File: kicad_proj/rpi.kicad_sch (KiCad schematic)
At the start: 9 parts, among them J4 Raspberry Pi SMT connector, J5 Conn_01x02, U3 CAT24C32WI-GT3

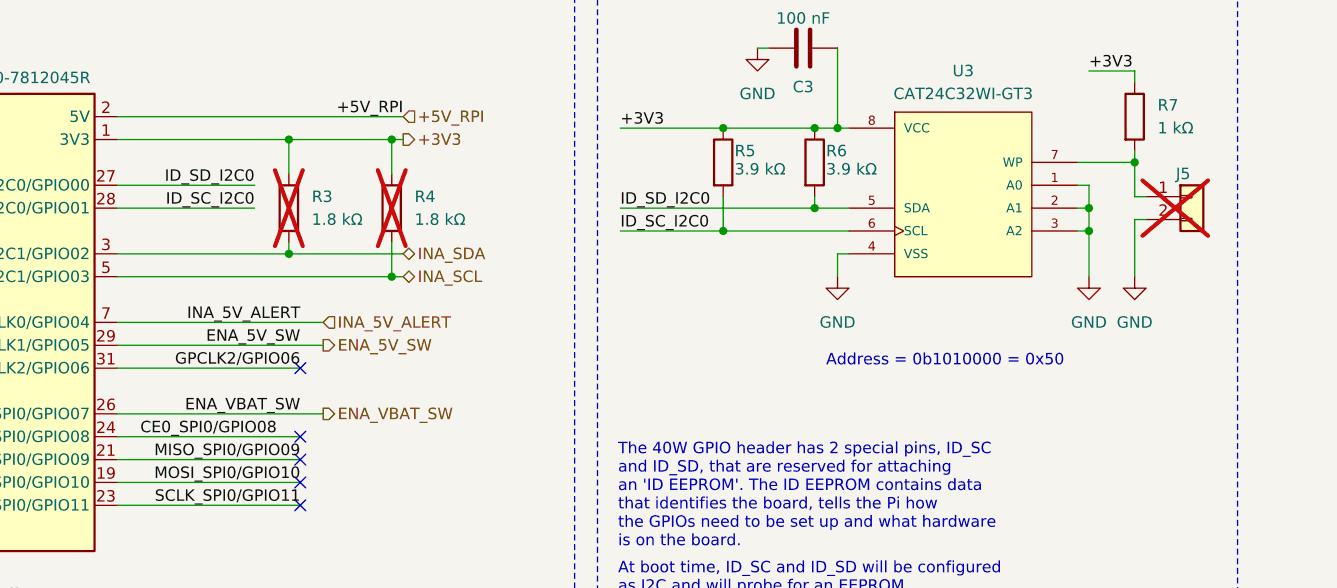
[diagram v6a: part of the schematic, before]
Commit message: feat: replace tht jumper by as solder bridge. feat: progress with layout.
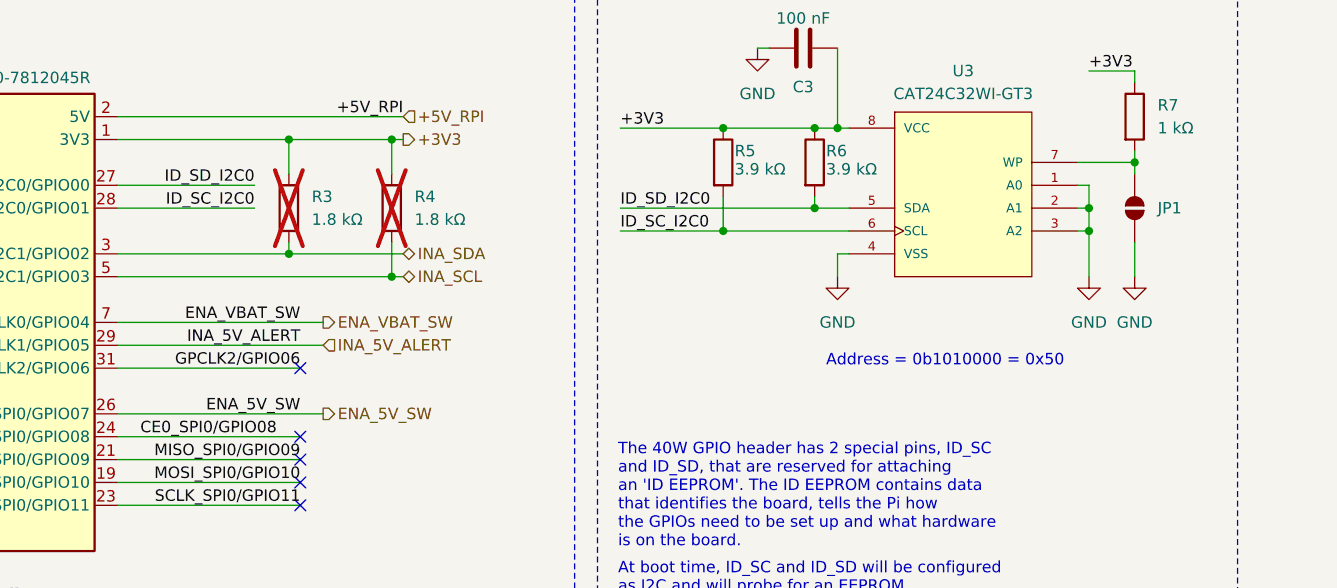
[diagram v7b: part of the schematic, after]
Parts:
- removed J5: Conn_01x02, Connector_PinHeader_2.54mm:PinHeader_1x02_P2.54mm_Vertical, symbol Connector_Generic:Conn_01x02
- added JP1: SolderJumper_2_Open, Jumper:SolderJumper-2_P1.3mm_Open_Pad1.0x1.5mm, symbol Jumper:SolderJumper_2_Open
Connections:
- net ENA_5V_SW: now also J4.26 (~{CE1}_SPI0/GPIO07); no longer J4.29 (GPCLK1/GPIO05)
- net ENA_VBAT_SW: now also J4.7 (GPCLK0/GPIO04); no longer J4.26 (~{CE1}_SPI0/GPIO07)
- net GND: now also JP1.1 (A)
- net INA_5V_ALERT: now also J4.29 (GPCLK1/GPIO05); no longer J4.7 (GPCLK0/GPIO04)
- net at R7.2, U3.7 (WP): now also JP1.2 (B)
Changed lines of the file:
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@@
 	(wire
 		(pts
-			(xy 236.22 63.5) (xy 234.95 63.5)
-		)
-		(stroke
-			(width 0)
-			(type default)
-		)
-	)
-	(wire
-		(pts
 			(xy 229.87 49.53) (xy 234.95 49.53)
 		)
@@
 	(wire
 		(pts
-			(xy 121.92 80.01) (xy 144.78 80.01)
-		)
-		(stroke
-			(width 0)
-			(type default)
-		)
-	)
-	(wire
-		(pts
 			(xy 33.02 77.47) (xy 55.88 77.47)
 		)
@@
 	(wire
 		(pts
-			(xy 234.95 66.04) (xy 234.95 72.39)
+			(xy 189.23 63.5) (xy 189.23 67.31)
 		)
 		(stroke
@@
 	(wire
 		(pts
-			(xy 189.23 63.5) (xy 189.23 67.31)
+			(xy 121.92 80.01) (xy 144.78 80.01)
 		)
 		(stroke
@@
 	(wire
 		(pts
+			(xy 121.92 77.47) (xy 144.78 77.47)
+		)
+		(stroke
+			(width 0)
+			(type default)
+		)
+	)
+	(wire
+		(pts
 			(xy 229.87 72.39) (xy 229.87 67.31)
 		)
@@
 	(wire
 		(pts
-			(xy 121.92 64.77) (xy 137.16 64.77)
+			(xy 234.95 68.58) (xy 234.95 72.39)
 		)
 		(stroke
@@
 	(wire
 		(pts
-			(xy 33.02 95.25) (xy 55.88 95.25)
+			(xy 121.92 87.63) (xy 144.78 87.63)
 		)
 		(stroke
@@
 	(wire
 		(pts
-			(xy 140.97 57.15) (xy 140.97 60.96)
+			(xy 121.92 64.77) (xy 137.16 64.77)
 		)
 		(stroke
@@
 	(wire
 		(pts
-			(xy 177.8 67.31) (xy 189.23 67.31)
+			(xy 33.02 95.25) (xy 55.88 95.25)
 		)
 		(stroke
@@
 	(wire
 		(pts
-			(xy 33.02 80.01) (xy 55.88 80.01)
+			(xy 140.97 57.15) (xy 140.97 60.96)
 		)
 		(stroke
@@
 	(wire
 		(pts
-			(xy 121.92 97.79) (xy 142.24 97.79)
+			(xy 177.8 67.31) (xy 189.23 67.31)
 		)
 		(stroke
@@
 	(wire
 		(pts
-			(xy 234.95 66.04) (xy 236.22 66.04)
+			(xy 33.02 80.01) (xy 55.88 80.01)
 		)
 		(stroke
@@
 	(wire
 		(pts
-			(xy 121.92 87.63) (xy 144.78 87.63)
+			(xy 121.92 97.79) (xy 142.24 97.79)
 		)
 		(stroke
@@
 	(wire
 		(pts
-			(xy 121.92 77.47) (xy 144.78 77.47)
+			(xy 234.95 60.96) (xy 234.95 59.69)
 		)
 		(stroke
@@
 	(wire
 		(pts
-			(xy 234.95 63.5) (xy 234.95 59.69)
-		)
-		(stroke
-			(width 0)
-			(type default)
-		)
-	)
-	(wire
-		(pts
 			(xy 201.93 72.39) (xy 201.93 69.85)
 		)
@@
 		)
 	)
-	(label "INA_5V_ALERT"
-		(at 142.24 77.47 180)
-		(effects
-			(font
-				(size 1.27 1.27)
-			)
-			(justify right bottom)
-		)
-	)
 	(label "GPIO12{slash}PWM0"
 		(at 33.02 54.61 0)
@@
 		)
 	)
-	(label "ENA_VBAT_SW"
-		(at 142.24 87.63 180)
-		(effects
-			(font
-				(size 1.27 1.27)
-			)
-			(justify right bottom)
-		)
-	)
 	(label "ID_SD_I2C0"
 		(at 137.16 62.23 180)
@@
 		)
 	)
+	(label "ENA_VBAT_SW"
+		(at 142.24 77.47 180)
+		(effects
+			(font
+				(size 1.27 1.27)
+			)
+			(justify right bottom)
+		)
+	)
+	(label "INA_5V_ALERT"
+		(at 142.24 80.01 180)
+		(effects
+			(font
+				(size 1.27 1.27)
+			)
+			(justify right bottom)
+		)
+	)
 	(label "ID_SD_I2C0"
 		(at 177.8 64.77 0)
@@
 		)
 	)
-	(label "INA_VBAT_ALERT"
-		(at 33.02 72.39 0)
+	(label "ENA_5V_SW"
+		(at 142.24 87.63 180)
 		(effects
 			(font
 				(size 1.27 1.27)
 			)
-			(justify left bottom)
+			(justify right bottom)
 		)
 	)
-	(label "GPIO15{slash}UART_RXD"
-		(at 33.02 64.77 0)
+	(label "INA_VBAT_ALERT"
+		(at 33.02 72.39 0)
 		(effects
 			(font
@@
 		)
 	)
-	(label "ENA_5V_SW"
-		(at 142.24 80.01 180)
+	(label "GPIO15{slash}UART_RXD"
+		(at 33.02 64.77 0)
 		(effects
 			(font
 				(size 1.27 1.27)
 			)
-			(justify right bottom)
+			(justify left bottom)
 		)
 	)
@@
 		)
 	)
-	(hierarchical_label "INA_VBAT_ALERT"
+	(hierarchical_label "INA_5V_ALERT"
 		(shape input)
-		(at 33.02 72.39 180)
+		(at 144.78 80.01 0)
 		(effects
 			(font
 				(size 1.27 1.27)
 			)
-			(justify right)
+			(justify left)
 		)
 	)
-	(hierarchical_label "INA_SCL"
-		(shape bidirectional)
-		(at 153.67 72.39 0)
+	(hierarchical_label "ENA_VBAT_SW"
+		(shape output)
+		(at 144.78 77.47 0)
 		(effects
 			(font
@@
 		)
 	)
-	(hierarchical_label "ENA_5V_SW"
-		(shape output)
-		(at 144.78 80.01 0)
+	(hierarchical_label "INA_VBAT_ALERT"
+		(shape input)
+		(at 33.02 72.39 180)
 		(effects
 			(font
 				(size 1.27 1.27)
 			)
-			(justify left)
+			(justify right)
 		)
 	)
-	(hierarchical_label "INA_5V_ALERT"
-		(shape input)
-		(at 144.78 77.47 0)
+	(hierarchical_label "INA_SCL"
+		(shape bidirectional)
+		(at 153.67 72.39 0)
 		(effects
 			(font
@@
 		)
 	)
-	(hierarchical_label "ENA_VBAT_SW"
+	(hierarchical_label "ENA_5V_SW"
 		(shape output)
 		(at 144.78 87.63 0)
@@
 	)
 	(symbol
-		(lib_id "Connector_Generic:Conn_01x02")
-		(at 241.3 63.5 0)
+		(lib_id "Jumper:SolderJumper_2_Open")
+		(at 234.95 64.77 90)
 		(unit 1)
-		(exclude_from_sim no)
+		(exclude_from_sim yes)
 		(in_bom no)
 		(on_board yes)
-		(dnp yes)
-		(property "Reference" "J5"
-			(at 239.522 60.96 0)
+		(dnp no)
+		(fields_autoplaced yes)
+		(property "Reference" "JP1"
+			(at 237.49 64.7699 90)
 			(effects
 				(font
 					(size 1.27 1.27)
 				)
-				(justify left)
+				(justify right)
 			)
 		)
-		(property "Value" "Conn_01x02"
-			(at 243.84 66.0399 0)
+		(property "Value" "SolderJumper_2_Open"
+			(at 237.49 66.0399 90)
 			(effects
 				(font
 					(size 1.27 1.27)
 				)
-				(justify left)
+				(justify right)
 				(hide yes)
 			)
 		)
-		(property "Footprint" "Connector_PinHeader_2.54mm:PinHeader_1x02_P2.54mm_Vertical"
-			(at 241.3 63.5 0)
+		(property "Footprint" "Jumper:SolderJumper-2_P1.3mm_Open_Pad1.0x1.5mm"
+			(at 234.95 64.77 0)
 			(effects
 				(font
@@
 		)
 		(property "Datasheet" "~"
-			(at 241.3 63.5 0)
+			(at 234.95 64.77 0)
 			(effects
 				(font
@@
 			)
 		)
-		(property "Description" "Generic connector, single row, 01x02, script generated (kicad-library-utils/schlib/autogen/connector/)"
-			(at 241.3 63.5 0)
+		(property "Description" "Solder Jumper, 2-pole, open"
+			(at 234.95 64.77 0)
 			(effects
 				(font
@@
 			(project ""
 				(path "/8692c5de-a943-41e8-8e29-f6c5e99cda34/014d6471-91bd-4d51-9996-105480561d0c"
-					(reference "J5")
+					(reference "JP1")
 					(unit 1)
 				)

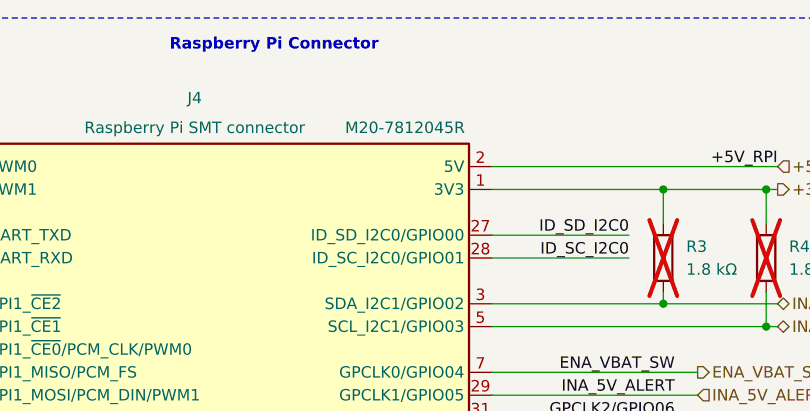
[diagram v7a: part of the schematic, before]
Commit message: fix: replace some components out of stock in lcsc
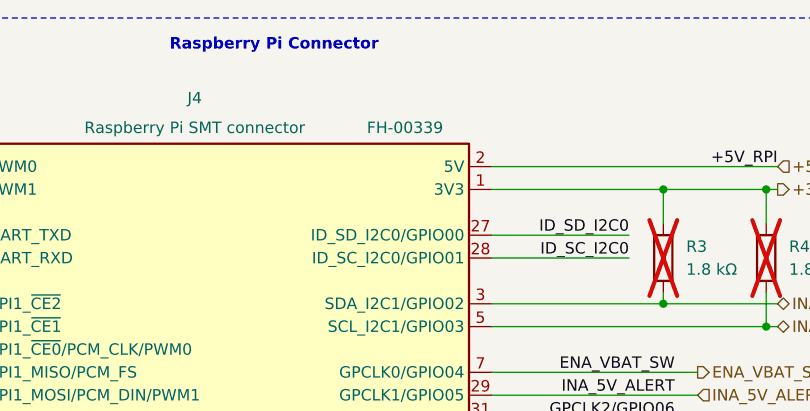
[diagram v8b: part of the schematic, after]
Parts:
- J4: manufacturer Harwin Inc. -> Liansheng; manufacturer_2 (none) -> Harwin Inc.; mpn M20-7812045R -> FH-00339; mpn_2 (none) -> M20-7812045R
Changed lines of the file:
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@@
 			)
 		)
-		(property "mpn" "M20-7812045R"
+		(property "mpn" "FH-00339"
 			(at 112.268 50.292 0)
 			(effects
@@
 			)
 		)
-		(property "manufacturer" "Harwin Inc."
+		(property "manufacturer" "Liansheng"
 			(at 88.9 76.2 0)
 			(effects
+				(font
+					(size 1.27 1.27)
+				)
+				(hide yes)
+			)
+		)
+		(property "mpn_2" "M20-7812045R"
+			(at 107.442 104.14 0)
+			(effects
+				(font
+					(size 1.27 1.27)
+				)
+				(hide yes)
+			)
+		)
+		(property "manufacturer_2" "Harwin Inc."
+			(at 88.9 76.2 0)
+			(effects
